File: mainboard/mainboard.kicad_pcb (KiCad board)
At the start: 2 copper layers, 91 x 100 mm, 126 parts, among them J1 Eurorack_Power, J10 H2, J11 CV3, J12 O3, J13 H3, J2 R1, J3 CV1, J4 R2, J5 O1, J6 H1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

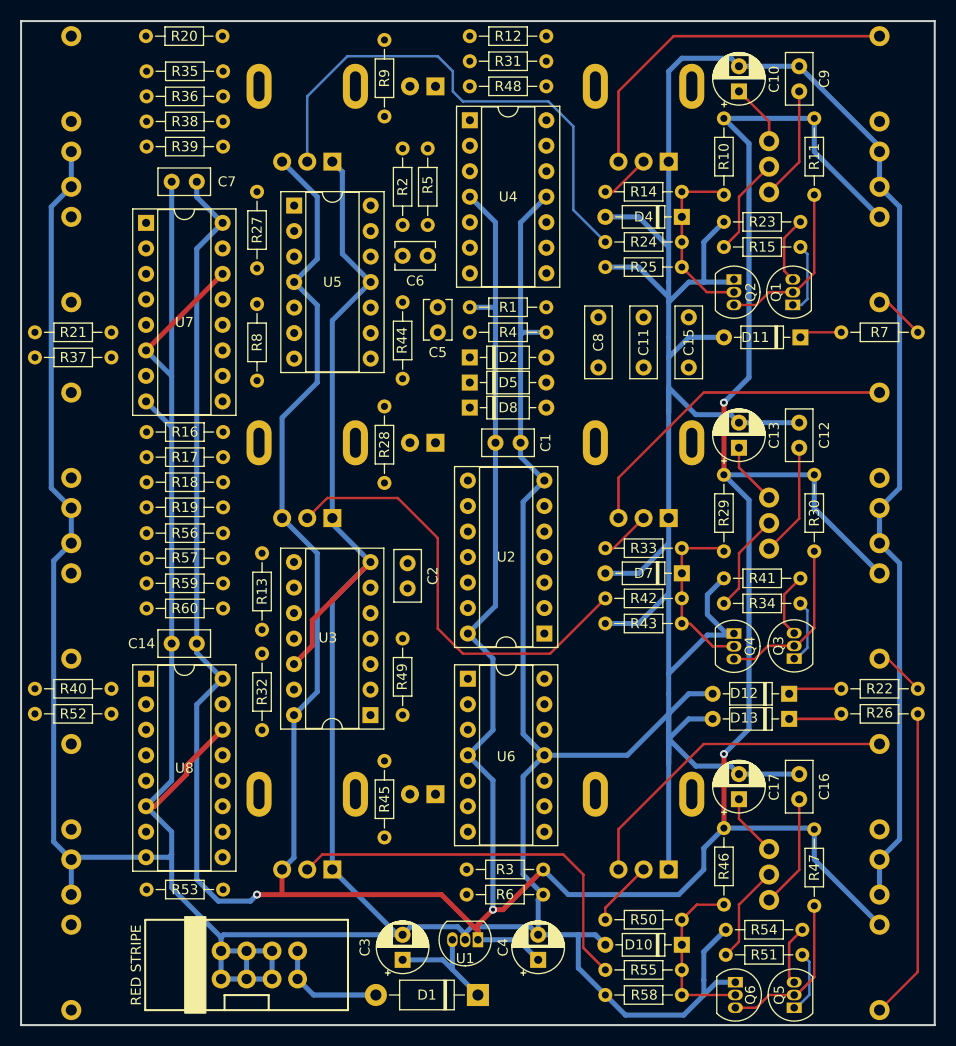
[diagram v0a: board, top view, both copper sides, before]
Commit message: Some more routing, moved D2, D5 and D8 to make it cleanr
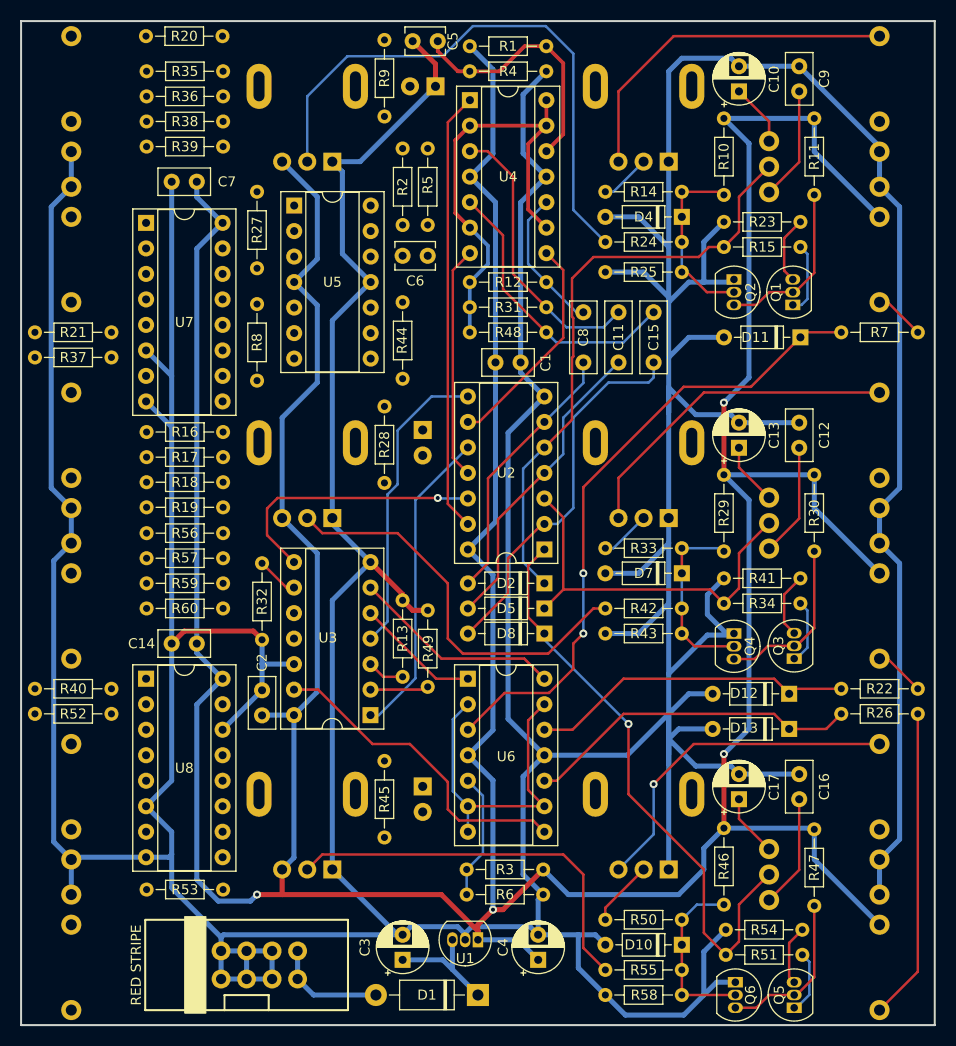
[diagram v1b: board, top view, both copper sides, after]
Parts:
- moved C5 29.0 mm to (55.5, 15.0), turned to 180 degrees
- moved R1 26.0 mm to (58.7, 15.5)
- moved R4 26.0 mm to (58.7, 18.0)
- moved R12 25.7 mm to (58.7, 39.0), turned to 0 degrees
- moved R31 25.7 mm to (58.7, 41.5), turned to 0 degrees
- moved R48 25.7 mm to (58.7, 44.0), turned to 0 degrees
- moved D2 23.7 mm to (66.1, 69.0), turned to 180 degrees
- moved D5 23.7 mm to (66.1, 71.5), turned to 180 degrees
- moved D8 23.7 mm to (66.1, 74.0), turned to 180 degrees
- moved C2 21.0 mm to (38.0, 82.2), turned to 90 degrees
- moved R13 14.3 mm to (52.0, 70.7), turned to -90 degrees
- moved R49 10.7 mm to (54.5, 71.7), turned to -90 degrees
- moved R32 9.00 mm to (38.0, 74.6)
- moved U2 8.38 mm to (66.1, 65.6)
- moved C1 8.00 mm to (61.2, 47.0)
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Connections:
- U2 pad 1: Net-(D2-Pad1) -> Net-(D8-Pad1)
- U2 pad 10: Net-(C15-Pad1) -> Out3
- U2 pad 11: Net-(D8-Pad1) -> Net-(U2-Pad11)
- U2 pad 12: Out3 -> Out2
- U2 pad 2: Net-(C8-Pad1) -> Net-(C15-Pad1)
- U2 pad 3: Net-(U2-Pad3) -> Net-(D5-Pad1)
- U2 pad 4: Out1 -> Net-(C11-Pad1)
- U2 pad 5: Net-(D5-Pad1) -> Net-(D2-Pad1)
- U2 pad 6: Net-(C11-Pad1) -> Net-(C8-Pad1)
- U2 pad 8: Out2 -> Out1
- U3 pad 1: Out1 -> Out3
- U3 pad 13: R1o -> R3o
- U3 pad 2: Net-(R13-Pad2) -> Net-(R49-Pad2)
- U3 pad 3: Net-(R32-Pad2) -> Net-(R13-Pad2)
- U3 pad 4: Out2 -> Out1
- U3 pad 5: R2o -> R1o
- U3 pad 6: R3o -> R2o
- U3 pad 8: Out3 -> Out2
- U3 pad 9: Net-(R49-Pad2) -> Net-(R32-Pad2)
- U4 pad 1: Vref -> Net-(U2-Pad13)
- U4 pad 10: Net-(C11-Pad2) -> Net-(C8-Pad2)
- U4 pad 12: Net-(C15-Pad2) -> Net-(C5-Pad1)
- U4 pad 14: Net-(U2-Pad13) -> Vref
- U4 pad 3: Net-(C5-Pad1) -> Net-(C11-Pad2)
- U4 pad 5: Net-(C8-Pad2) -> Net-(C15-Pad2)
- U4 pad 7: Net-(U2-Pad3) -> Net-(U2-Pad11)
- U6 pad 1: CmpVref -> R1o
- U6 pad 10: Net-(D12-Pad1) -> Net-(D13-Pad1)
- U6 pad 12: Net-(D13-Pad1) -> Net-(D12-Pad1)
- U6 pad 14: R3o -> R2o
- U6 pad 3: Net-(R3-Pad2) -> Net-(D11-Pad1)
- U6 pad 5: Net-(D11-Pad1) -> Net-(R3-Pad2)
- U6 pad 7: R1o -> CmpVref
- U6 pad 8: R2o -> R3o
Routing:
- net Net-(D11-Pad1): track 4.28 -> 63.6 mm, vias 0 -> 2
- net Net-(D2-Pad1): track 9.86 -> 59.7 mm
- net Net-(D8-Pad1): track 9.79 -> 59.0 mm, vias 0 -> 1
- net Vref: track 0.00 -> 45.1 mm
- net Net-(U2-Pad13): track 0.00 -> 43.9 mm
- net Net-(C15-Pad1): track 0.00 -> 37.9 mm
- net CmpVref: track 0.00 -> 33.1 mm
- net R3o: track 0.00 -> 32.4 mm
- net Out3: track 0.00 -> 31.2 mm
- net Net-(C11-Pad1): track 0.00 -> 30.7 mm
- net Out1: track 0.00 -> 30.3 mm
- net Net-(D5-Pad1): track 9.86 -> 38.9 mm
- net Net-(C15-Pad2): track 0.00 -> 28.5 mm
- net Net-(C11-Pad2): track 0.00 -> 28.4 mm
- net Net-(D13-Pad1): track 5.40 -> 33.6 mm
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
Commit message: Routing
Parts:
- D10, D11, D12, D13, D4, D7: value 1N4148 -> BAT85
- U6: value TL074 -> LM324
- moved R27 18.5 mm to (52.0, 41.5)
- moved R44 14.1 mm to (38.0, 39.0), turned to 90 degrees
- moved R19 10.6 mm to (34.1, 54.0), turned to 180 degrees
- moved R35 9.11 mm to (34.1, 23.0), turned to 180 degrees
- moved R38 9.11 mm to (34.1, 18.0), turned to 180 degrees
- moved R56 9.11 mm to (34.1, 69.0), turned to 180 degrees
- moved R59 9.11 mm to (34.1, 64.0), turned to 180 degrees
- moved R8 7.64 mm to (38.0, 41.2), turned to -90 degrees
- moved R36 7.62 mm to (34.1, 20.5), turned to 180 degrees
- moved R57 7.62 mm to (34.1, 66.5), turned to 180 degrees
- moved D6 3.05 mm to (54.0, 56.8), turned to 90 degrees
- moved R16 2.57 mm to (26.5, 56.5)
- moved R17 2.57 mm to (26.5, 59.0)
- moved R18 2.57 mm to (26.5, 61.5)
- moved D9 2.55 mm to (54.0, 91.8), turned to 90 degrees
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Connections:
- U5 pad 1: Vref2 -> Hav3
- U5 pad 12: Vref2 -> Net-(C6-Pad1)
- U5 pad 13: Net-(R44-Pad1) -> Vref2
- U5 pad 14: Hav3 -> Vref2
- U5 pad 2: Vref2 -> Net-(R44-Pad1)
- U5 pad 3: Net-(C6-Pad1) -> Vref2
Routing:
- net Hav3: track 0.00 -> 165.0 mm, vias 0 -> 3
- net Hav2: track 0.00 -> 138.9 mm, vias 0 -> 1
- net Hav1: track 0.00 -> 121.1 mm, vias 0 -> 8
- net Out1: track 30.3 -> 121.8 mm, vias 0 -> 2
- net Out3: track 31.2 -> 109.7 mm, vias 0 -> 5
- net Net-(R44-Pad1): track 0.00 -> 51.0 mm, vias 0 -> 3
- net Net-(R49-Pad2): track 5.81 -> 54.2 mm, vias 0 -> 1
- net Net-(R27-Pad1): track 0.00 -> 47.4 mm
- net GND: track 807.6 -> 854.9 mm, vias 0 -> 1
- net Net-(R32-Pad2): track 4.18 -> 43.7 mm, vias 0 -> 1
- net Net-(R13-Pad2): track 3.72 -> 38.4 mm, vias 0 -> 1
- net Net-(R16-Pad2): track 0.00 -> 34.5 mm, vias 0 -> 1
- net Out2: track 26.9 -> 59.0 mm, vias 1 -> 3
- net Net-(R38-Pad1): track 0.00 -> 29.6 mm
- net Net-(R59-Pad1): track 0.00 -> 29.0 mm
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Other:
- board text added: "circuit and pcb by Neil Massey inspired by Old Mr Grassi by Ciat-Lonbarde thanks to Chester Winowiecki"
- board text added: "panel components other side"
- board text added: "panel components this side"

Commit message: Panel commit
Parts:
- moved J10 0.50 mm to (19.5, 71.5)
- moved J12 0.50 mm to (19.5, 90.0)
- moved J13 0.50 mm to (19.5, 106.5)
- moved J5 0.50 mm to (19.5, 19.5)
- moved J6 0.50 mm to (19.5, 36.0)
- moved J9 0.50 mm to (19.5, 55.0)
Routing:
- net Net-(J9-PadT): track 5.07 -> 5.57 mm
- net Net-(J6-PadT): track 4.86 -> 5.36 mm
- net Net-(J12-PadT): track 4.86 -> 5.36 mm
- net Net-(J10-PadT): track 4.86 -> 5.36 mm
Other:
- board text added: "circuit, pcb: Neil Massey inspired: Old Mr Grassi thanks: Chester Winowiecki"
- board text removed: "circuit and pcb by Neil Massey inspired by Old Mr Grassi by Ciat-Lonbarde thanks to Chester Winowiecki"

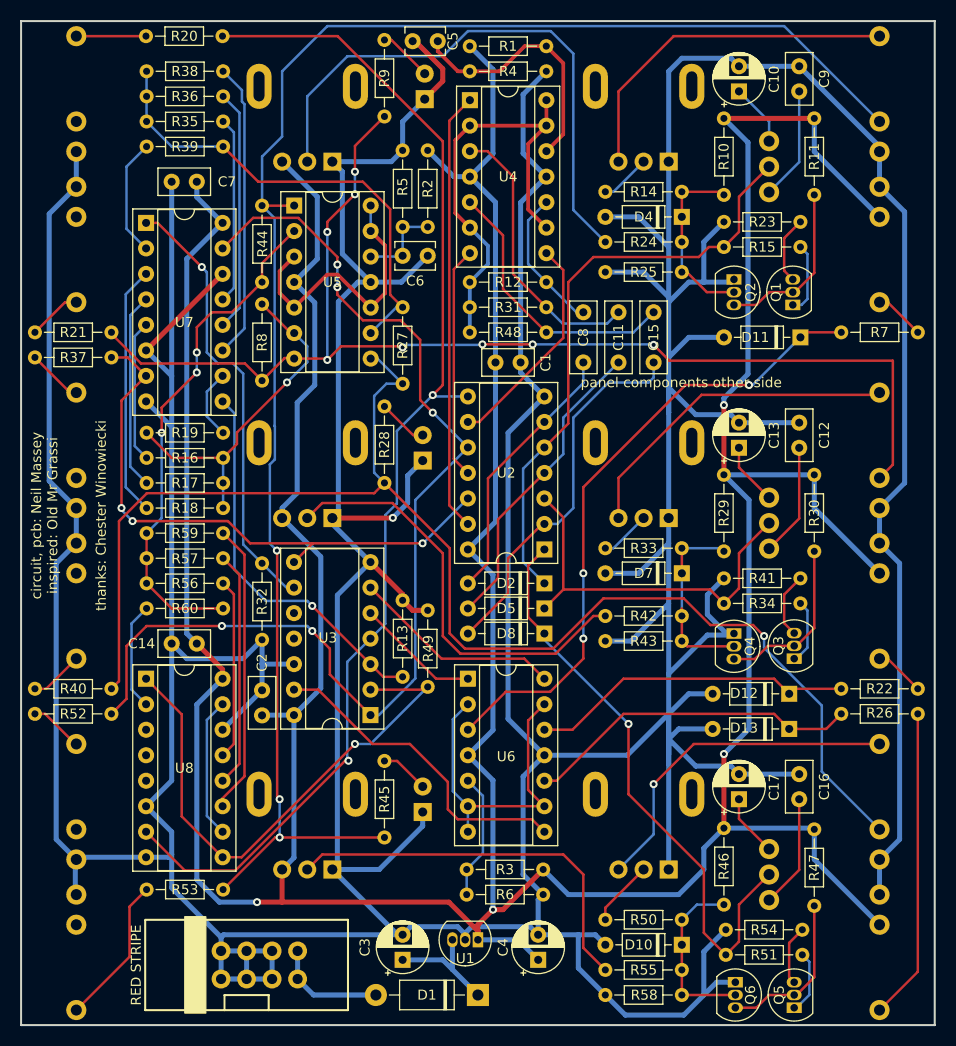
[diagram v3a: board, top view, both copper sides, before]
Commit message: Traces corrected
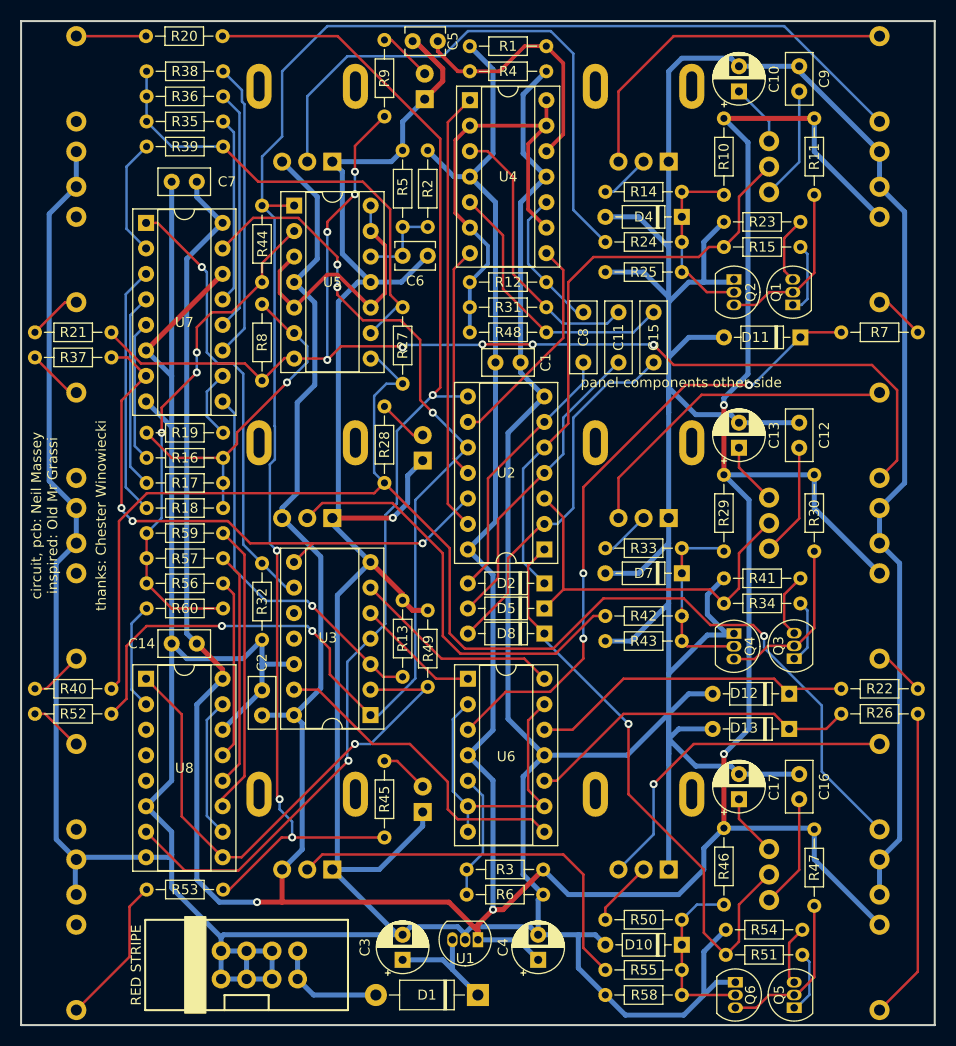
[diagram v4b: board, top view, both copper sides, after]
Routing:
- net Hav1: track 121.1 -> 120.0 mm
- net Net-(C15-Pad1): track 37.9 -> 37.0 mm
- net +9V: track 467.9 -> 468.6 mm
- net Hav3: track 165.0 -> 165.5 mm

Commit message: Panel tweaks
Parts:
- moved J10 0.50 mm to (20.0, 71.5)
- moved J11 0.50 mm to (99.0, 90.0)
- moved J12 0.50 mm to (20.0, 90.0)
- moved J13 0.50 mm to (20.0, 106.5)
- moved J2 0.50 mm to (99.0, 36.0)
- moved J3 0.50 mm to (99.0, 19.5)
- moved J4 0.50 mm to (99.0, 71.5)
- moved J5 0.50 mm to (20.0, 19.5)
- moved J6 0.50 mm to (20.0, 36.0)
- moved J7 0.50 mm to (99.0, 106.5)
- moved J8 0.50 mm to (99.0, 55.0)
- moved J9 0.50 mm to (20.0, 55.0)
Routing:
- net GND: track 855.3 -> 856.3 mm
- net +9V: track 468.6 -> 468.0 mm
- net Hav3: track 165.5 -> 165.0 mm
- net Net-(J9-PadT): track 5.57 -> 6.07 mm
- net Net-(J8-PadT): track 33.5 -> 33.0 mm
- net Net-(J7-PadT): track 31.1 -> 31.6 mm
- net Net-(J6-PadT): track 5.36 -> 5.86 mm
- net Net-(J5-PadT): track 6.94 -> 6.44 mm
- net Net-(J4-PadT): track 5.05 -> 5.55 mm
- net Net-(J3-PadT): track 35.3 -> 34.8 mm
- net Net-(J2-PadT): track 5.05 -> 5.55 mm
- net Net-(J12-PadT): track 5.36 -> 5.86 mm
- net Net-(J11-PadT): track 34.1 -> 33.6 mm
- net Net-(J10-PadT): track 5.36 -> 5.86 mm
